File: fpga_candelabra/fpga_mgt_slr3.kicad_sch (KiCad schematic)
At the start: 1 part, among them U1 XCVU13P-B2104

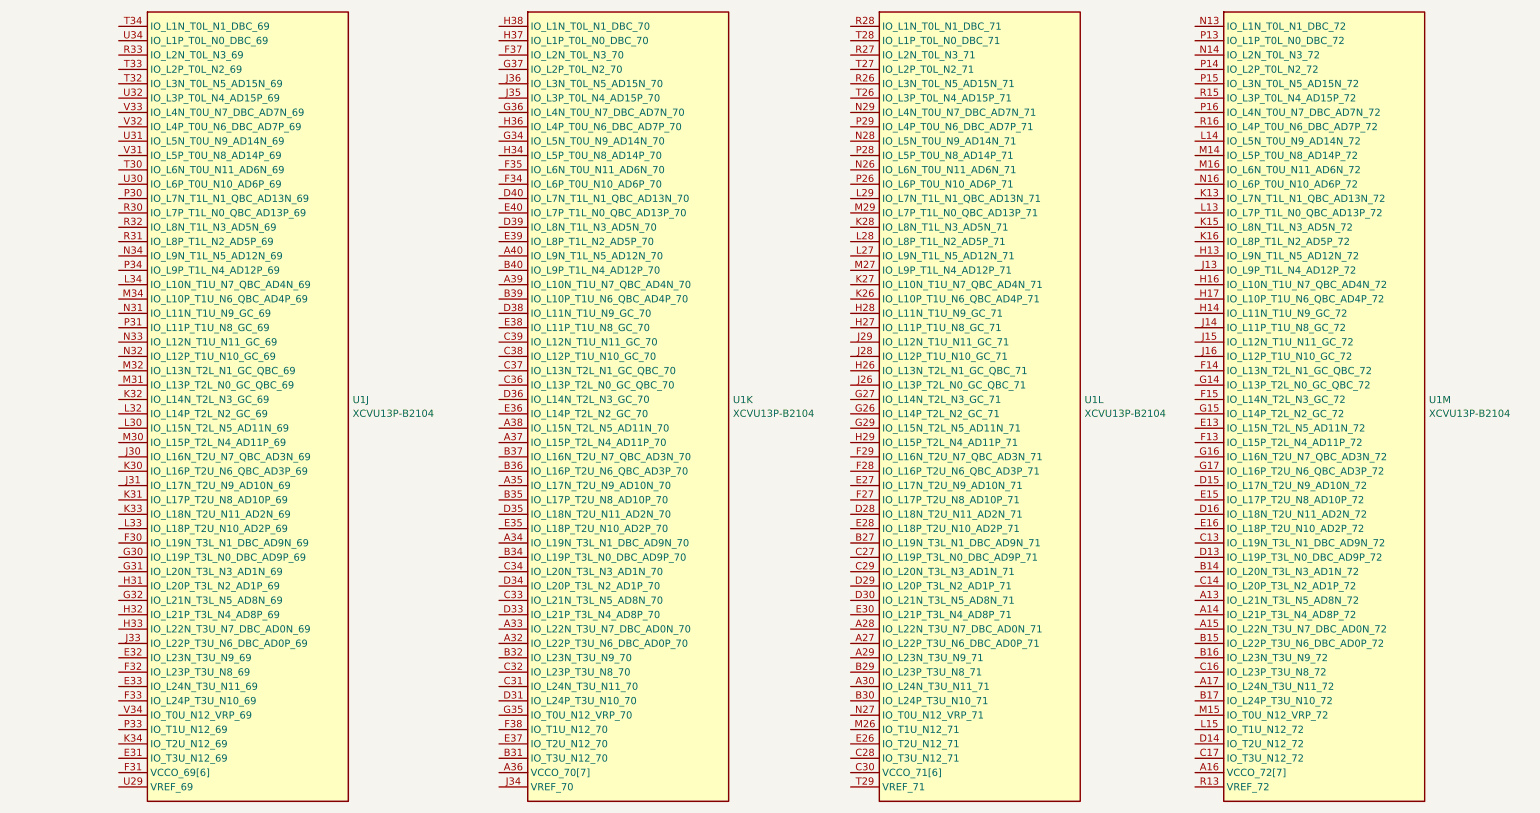
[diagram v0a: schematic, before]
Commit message: fpga_candelabra: reorganize fpga io and mgt by SLR
- Rename sch sheets
- Add prelimary DDR and PCIE Bank/Quad allocation

Signed-off-by: Yichuan Gao <gaoyichuan000@gmail.com>
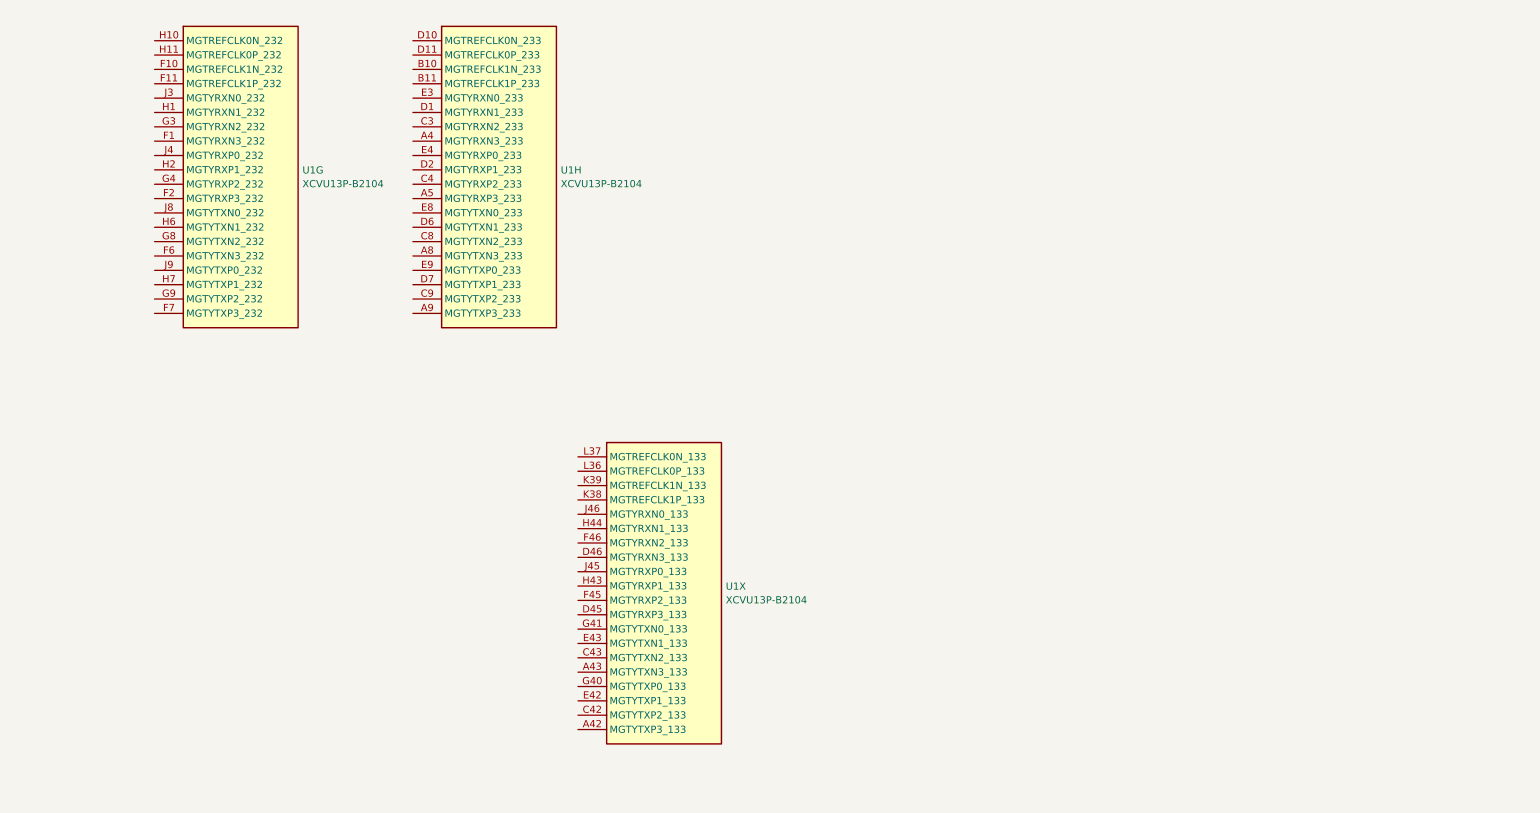
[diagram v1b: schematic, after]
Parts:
- removed U1: XCVU13P-B2104, CHIPSAlliance_Package_BGA:Xilinx_FHGB2104_VU13P_PkgLength, symbol CHIPSAlliance_FPGA_Xilinx_Virtex_UltraScale_Plus:XCVU13P-B2104
- added U1: XCVU13P-B2104, CHIPSAlliance_Package_BGA:Xilinx_FHGB2104_VU13P_PkgLength, symbol CHIPSAlliance_FPGA_Xilinx_Virtex_UltraScale_Plus:XCVU13P-B2104

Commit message: candelabra: add i-pex extension ports, remove FMC1
* update bank/mgt allocation
* add basic pcb floorplanning

Signed-off-by: Yichuan Gao <gaoyichuan000@gmail.com>
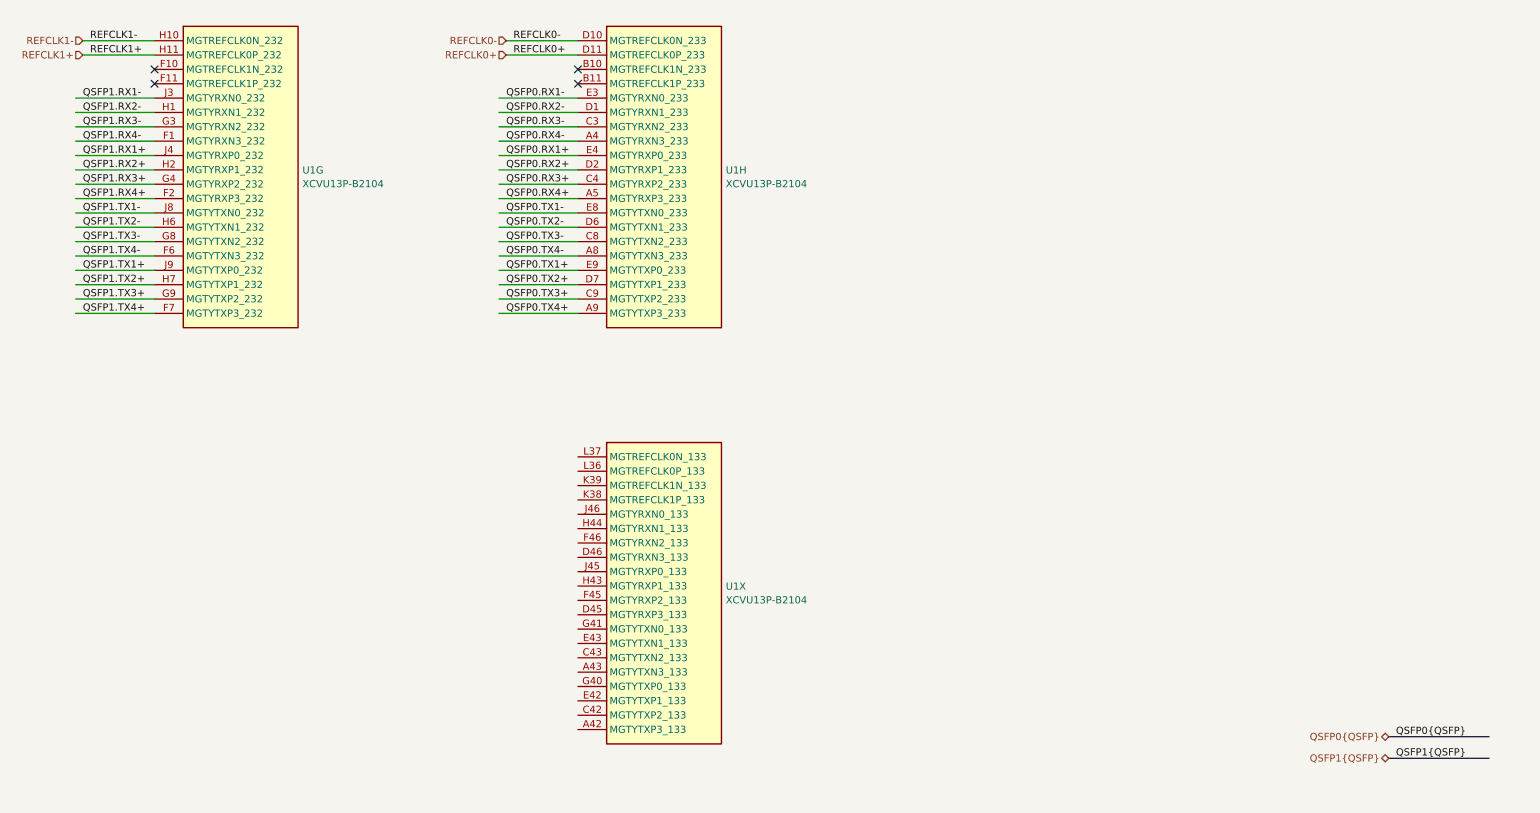
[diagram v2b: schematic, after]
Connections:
- net QSFP1.RX4-: now reaches U1.F1 (MGTYRXN3_232)
- net QSFP1.RX4+: now reaches U1.F2 (MGTYRXP3_232)
- net QSFP1.TX4-: now reaches U1.F6 (MGTYTXN3_232)
- net QSFP1.TX4+: now reaches U1.F7 (MGTYTXP3_232)
- net QSFP1.RX3-: now reaches U1.G3 (MGTYRXN2_232)
- net QSFP1.RX3+: now reaches U1.G4 (MGTYRXP2_232)
- net QSFP1.TX3-: now reaches U1.G8 (MGTYTXN2_232)
- net QSFP1.TX3+: now reaches U1.G9 (MGTYTXP2_232)
- net QSFP1.RX2-: now reaches U1.H1 (MGTYRXN1_232)
- net REFCLK1-: now reaches U1.H10 (MGTREFCLK0N_232)
- net REFCLK1+: now reaches U1.H11 (MGTREFCLK0P_232)
- net QSFP1.RX2+: now reaches U1.H2 (MGTYRXP1_232)
- net QSFP1.TX2-: now reaches U1.H6 (MGTYTXN1_232)
- net QSFP1.TX2+: now reaches U1.H7 (MGTYTXP1_232)
- net QSFP1.RX1-: now reaches U1.J3 (MGTYRXN0_232)
- net QSFP1.RX1+: now reaches U1.J4 (MGTYRXP0_232)
- net QSFP1.TX1-: now reaches U1.J8 (MGTYTXN0_232)
- net QSFP1.TX1+: now reaches U1.J9 (MGTYTXP0_232)
- net QSFP0.RX4-: now reaches U1.A4 (MGTYRXN3_233)
- net QSFP0.RX4+: now reaches U1.A5 (MGTYRXP3_233)
- net QSFP0.TX4-: now reaches U1.A8 (MGTYTXN3_233)
- net QSFP0.TX4+: now reaches U1.A9 (MGTYTXP3_233)
- net QSFP0.RX3-: now reaches U1.C3 (MGTYRXN2_233)
- net QSFP0.RX3+: now reaches U1.C4 (MGTYRXP2_233)
- net QSFP0.TX3-: now reaches U1.C8 (MGTYTXN2_233)
- net QSFP0.TX3+: now reaches U1.C9 (MGTYTXP2_233)
- net QSFP0.RX2-: now reaches U1.D1 (MGTYRXN1_233)
- net REFCLK0-: now reaches U1.D10 (MGTREFCLK0N_233)
- net REFCLK0+: now reaches U1.D11 (MGTREFCLK0P_233)
- net QSFP0.RX2+: now reaches U1.D2 (MGTYRXP1_233)
- net QSFP0.TX2-: now reaches U1.D6 (MGTYTXN1_233)
- net QSFP0.TX2+: now reaches U1.D7 (MGTYTXP1_233)
- net QSFP0.RX1-: now reaches U1.E3 (MGTYRXN0_233)
- net QSFP0.RX1+: now reaches U1.E4 (MGTYRXP0_233)
- net QSFP0.TX1-: now reaches U1.E8 (MGTYTXN0_233)
- net QSFP0.TX1+: now reaches U1.E9 (MGTYTXP0_233)
- no-connect marks 0 -> 4
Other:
- moved on the sheet: U1H

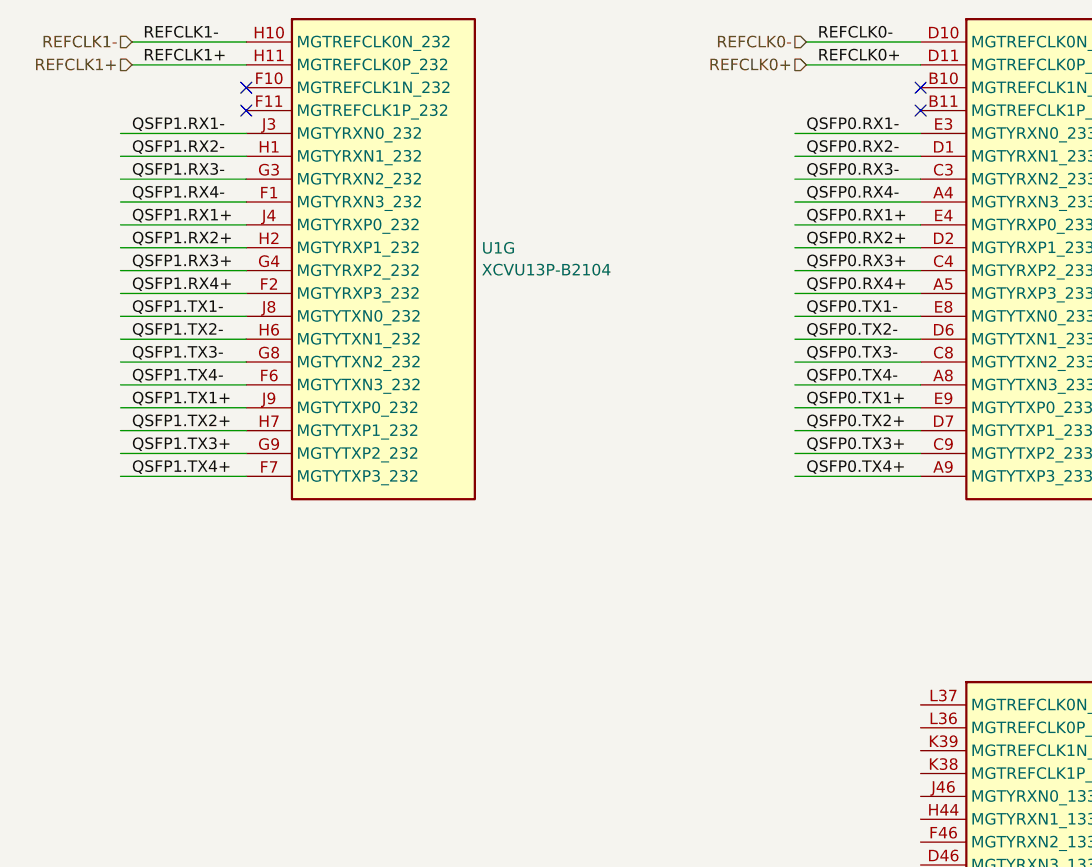
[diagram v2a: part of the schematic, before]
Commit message: fpga_candelabra: major revision
* Finish DDR4 & QSFP+ & PCIe layout
* Change FMC to LPC
* Add mikroBUS extension
* 12V input & PDN updates
* FPGA config updates

Signed-off-by: Yichuan Gao <gaoyichuan000@gmail.com>
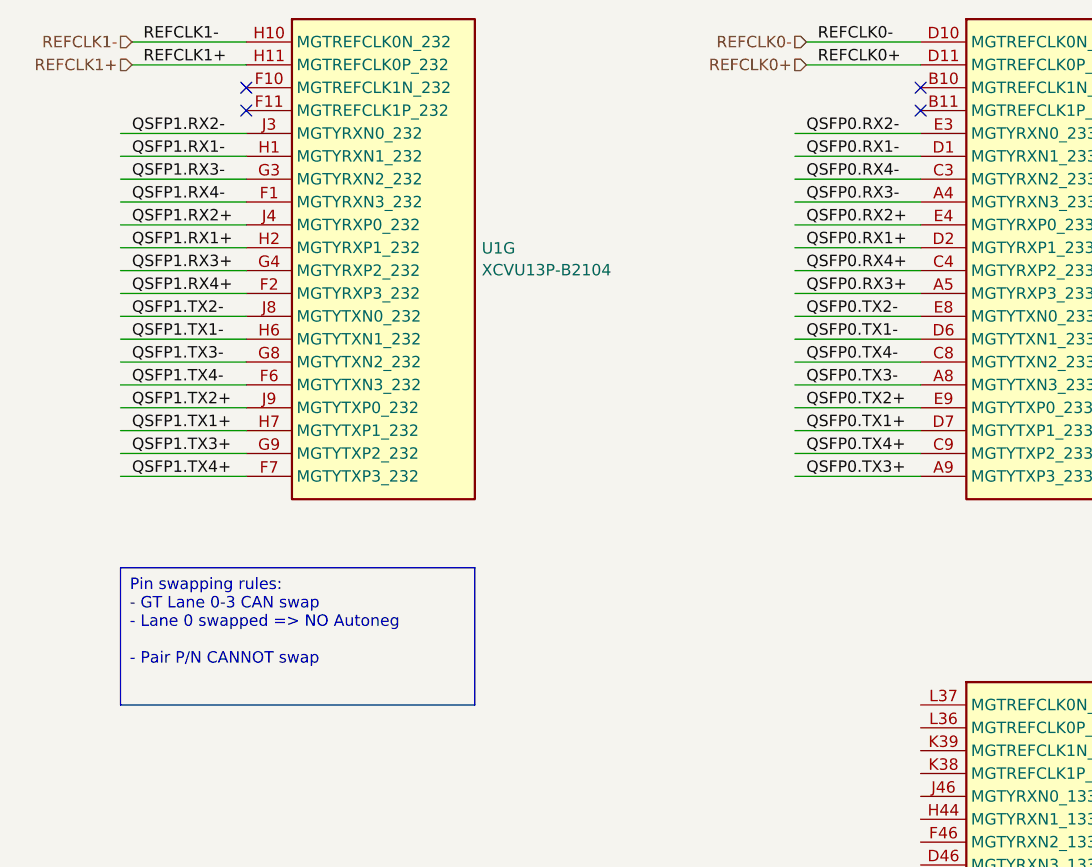
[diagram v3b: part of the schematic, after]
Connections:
- net QSFP0.RX1+: now also U1.D2 (MGTYRXP1_233); no longer U1.E4 (MGTYRXP0_233)
- net QSFP0.RX1-: now also U1.D1 (MGTYRXN1_233); no longer U1.E3 (MGTYRXN0_233)
- net QSFP0.RX2+: now also U1.E4 (MGTYRXP0_233); no longer U1.D2 (MGTYRXP1_233)
- net QSFP0.RX2-: now also U1.E3 (MGTYRXN0_233); no longer U1.D1 (MGTYRXN1_233)
- net QSFP0.RX3+: now also U1.A5 (MGTYRXP3_233); no longer U1.C4 (MGTYRXP2_233)
- net QSFP0.RX3-: now also U1.A4 (MGTYRXN3_233); no longer U1.C3 (MGTYRXN2_233)
- net QSFP0.RX4+: now also U1.C4 (MGTYRXP2_233); no longer U1.A5 (MGTYRXP3_233)
- net QSFP0.RX4-: now also U1.C3 (MGTYRXN2_233); no longer U1.A4 (MGTYRXN3_233)
- net QSFP0.TX1+: now also U1.D7 (MGTYTXP1_233); no longer U1.E9 (MGTYTXP0_233)
- net QSFP0.TX1-: now also U1.D6 (MGTYTXN1_233); no longer U1.E8 (MGTYTXN0_233)
- net QSFP0.TX2+: now also U1.E9 (MGTYTXP0_233); no longer U1.D7 (MGTYTXP1_233)
- net QSFP0.TX2-: now also U1.E8 (MGTYTXN0_233); no longer U1.D6 (MGTYTXN1_233)
- net QSFP0.TX3+: now also U1.A9 (MGTYTXP3_233); no longer U1.C9 (MGTYTXP2_233)
- net QSFP0.TX3-: now also U1.A8 (MGTYTXN3_233); no longer U1.C8 (MGTYTXN2_233)
- net QSFP0.TX4+: now also U1.C9 (MGTYTXP2_233); no longer U1.A9 (MGTYTXP3_233)
- net QSFP0.TX4-: now also U1.C8 (MGTYTXN2_233); no longer U1.A8 (MGTYTXN3_233)
- net QSFP1.RX1+: now also U1.H2 (MGTYRXP1_232); no longer U1.J4 (MGTYRXP0_232)
- net QSFP1.RX1-: now also U1.H1 (MGTYRXN1_232); no longer U1.J3 (MGTYRXN0_232)
- net QSFP1.RX2+: now also U1.J4 (MGTYRXP0_232); no longer U1.H2 (MGTYRXP1_232)
- net QSFP1.RX2-: now also U1.J3 (MGTYRXN0_232); no longer U1.H1 (MGTYRXN1_232)
- net QSFP1.TX1+: now also U1.H7 (MGTYTXP1_232); no longer U1.J9 (MGTYTXP0_232)
- net QSFP1.TX1-: now also U1.H6 (MGTYTXN1_232); no longer U1.J8 (MGTYTXN0_232)
- net QSFP1.TX2+: now also U1.J9 (MGTYTXP0_232); no longer U1.H7 (MGTYTXP1_232)
- net QSFP1.TX2-: now also U1.J8 (MGTYTXN0_232); no longer U1.H6 (MGTYTXN1_232)
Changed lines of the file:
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@@
+		)
+	)
+	(text_box "Pin swapping rules:\n- GT Lane 0-3 CAN swap\n- Lane 0 swapped => NO Autoneg\n\n- Pair P/N CANNOT swap"
+		(exclude_from_sim no)
+		(at 31.75 92.71 0)
+		(size 39.37 15.24)
+		(stroke
+			(width 0)
+			(type default)
+		)
+		(fill
+			(type none)
+		)
+		(effects
+			(font
+				(size 1.27 1.27)
+			)
+			(justify left top)
 		)
 	)
 	(label "QSFP1.RX2+"
-		(at 33.02 57.15 0)
+		(at 33.02 54.61 0)
 		(fields_autoplaced yes)
 		(effects
@@
 	)
 	(label "QSFP0.RX2+"
-		(at 107.95 57.15 0)
+		(at 107.95 54.61 0)
 		(fields_autoplaced yes)
 		(effects
@@
 	)
 	(label "QSFP0.TX1-"
-		(at 107.95 64.77 0)
+		(at 107.95 67.31 0)
 		(fields_autoplaced yes)
 		(effects
@@
 	)
 	(label "QSFP0.TX2+"
-		(at 107.95 77.47 0)
+		(at 107.95 74.93 0)
 		(fields_autoplaced yes)
 		(effects
@@
 	)
 	(label "QSFP0.RX4-"
-		(at 107.95 52.07 0)
+		(at 107.95 49.53 0)
 		(fields_autoplaced yes)
 		(effects
@@
 	)
 	(label "QSFP0.TX2-"
-		(at 107.95 67.31 0)
+		(at 107.95 64.77 0)
 		(fields_autoplaced yes)
 		(effects
@@
 	)
 	(label "QSFP1.RX1+"
-		(at 33.02 54.61 0)
+		(at 33.02 57.15 0)
 		(fields_autoplaced yes)
 		(effects
@@
 	)
 	(label "QSFP0.TX4+"
-		(at 107.95 82.55 0)
+		(at 107.95 80.01 0)
 		(fields_autoplaced yes)
 		(effects
@@
 	)
 	(label "QSFP1.RX2-"
-		(at 33.02 46.99 0)
+		(at 33.02 44.45 0)
 		(fields_autoplaced yes)
 		(effects
@@
 	)
 	(label "QSFP0.RX1+"
-		(at 107.95 54.61 0)
+		(at 107.95 57.15 0)
 		(fields_autoplaced yes)
 		(effects
@@
 	)
 	(label "QSFP0.TX4-"
-		(at 107.95 72.39 0)
+		(at 107.95 69.85 0)
 		(fields_autoplaced yes)
 		(effects
@@
 	)
 	(label "QSFP1.TX1+"
-		(at 33.02 74.93 0)
+		(at 33.02 77.47 0)
 		(fields_autoplaced yes)
 		(effects
@@
 	)
 	(label "QSFP0.TX1+"
-		(at 107.95 74.93 0)
+		(at 107.95 77.47 0)
 		(fields_autoplaced yes)
 		(effects
@@
 	)
 	(label "QSFP0.TX3+"
-		(at 107.95 80.01 0)
+		(at 107.95 82.55 0)
 		(fields_autoplaced yes)
 		(effects
@@
 	)
 	(label "QSFP0.RX3+"
-		(at 107.95 59.69 0)
+		(at 107.95 62.23 0)
 		(fields_autoplaced yes)
 		(effects
@@
 	)
 	(label "QSFP1.TX1-"
-		(at 33.02 64.77 0)
+		(at 33.02 67.31 0)
 		(fields_autoplaced yes)
 		(effects
@@
 	)
 	(label "QSFP1.TX2+"
-		(at 33.02 77.47 0)
+		(at 33.02 74.93 0)
 		(fields_autoplaced yes)
 		(effects
@@
 	)
 	(label "QSFP0.TX3-"
-		(at 107.95 69.85 0)
+		(at 107.95 72.39 0)
 		(fields_autoplaced yes)
 		(effects
@@
 	)
 	(label "QSFP1.RX1-"
-		(at 33.02 44.45 0)
+		(at 33.02 46.99 0)
 		(fields_autoplaced yes)
 		(effects
@@
 	)
 	(label "QSFP0.RX4+"
-		(at 107.95 62.23 0)
+		(at 107.95 59.69 0)
 		(fields_autoplaced yes)
 		(effects
@@
 	)
 	(label "QSFP1.TX2-"
-		(at 33.02 67.31 0)
+		(at 33.02 64.77 0)
 		(fields_autoplaced yes)
 		(effects
@@
 	)
 	(label "QSFP0.RX2-"
-		(at 107.95 46.99 0)
+		(at 107.95 44.45 0)
 		(fields_autoplaced yes)
 		(effects
@@
 	)
 	(label "QSFP0.RX3-"
-		(at 107.95 49.53 0)
+		(at 107.95 52.07 0)
 		(fields_autoplaced yes)
 		(effects
@@
 	)
 	(label "QSFP0.RX1-"
-		(at 107.95 44.45 0)
-		(fields_autoplaced yes)
-		(effects
+		(at 107.95 46.99 0)
+		(fields_autoplaced yes)
+		(effects
